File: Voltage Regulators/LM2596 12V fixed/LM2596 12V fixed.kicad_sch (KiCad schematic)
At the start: 5 parts, among them U1 LM2596S-12

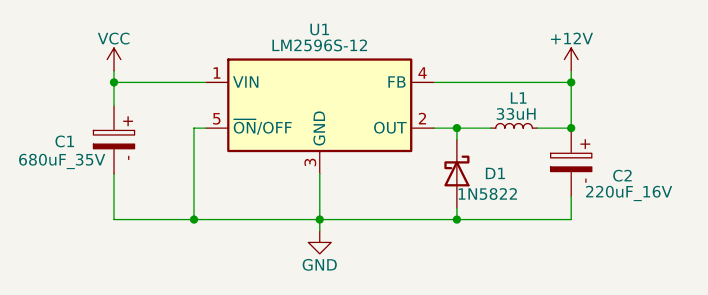
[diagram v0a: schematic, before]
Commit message: Edited 1N5822 to 1N5824
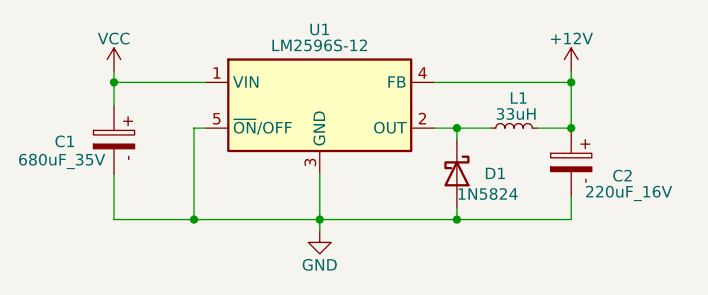
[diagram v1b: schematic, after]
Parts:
- D1: value 1N5822 -> 1N5824
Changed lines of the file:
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@@
 			)
 		)
-		(property "Value" "1N5822"
+		(property "Value" "1N5824"
 			(at 171.45 119.126 90)
 			(effects
